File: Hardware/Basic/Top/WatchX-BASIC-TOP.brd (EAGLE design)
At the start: 0 parts

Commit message: followed along with Take 001
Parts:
- added C10, C11: 300p, LinnesLab-Passives:C0603
- added C12: 10u, LinnesLab-Passives:C0805
- added C13, C15, C17, C18, C19: 2.2uF, LinnesLab-Passives:C0402
- added C14: 100n, LinnesLab-Passives:C0603
- added C16: 10uF, LinnesLab-Passives:C0603
- added C2, C5, C6, C7: 1u, LinnesLab-Passives:C0603
- added C20, C21: 4.7u, LinnesLab-Passives:C0603
- added C8, C9: (no value), LinnesLab-Passives:C0603
- added CHRG2: MCP73831, LinnesLab-Power:SOT23-5
- added CORTEX1: CORTEX_DEBUG_PTH, LinnesLab-Connectors:2X5-PTH-1.27MM
- added D1, D4, D5: (no value), LinnesLab-DiscreteSemi:USC
- added J2: (no value), LinnesLab-Connectors:1X02
- added L2: 10u, LinnesLab-Passives:L0603
- added LDO2: MIC5504, LinnesLab-Power:SOT23-5
- added LED3: RED, LinnesLab-LED:LED-0603
- added LED4: BLUE, LinnesLab-LED:LED-0603
- added R11: (no value), LinnesLab-Passives:R0603
- added R12, R13, R14, R15: 100k, LinnesLab-Passives:R0603
- added R3, R4: 1k, LinnesLab-Passives:R0603
- added R5, R6, R8, R9: 10k, LinnesLab-Passives:R0603
- added R7: 390k, LinnesLab-Passives:R0603
- added SD2: (no value), LinnesLab-Connectors:MICROSD
- added SW1, SW2: SWITCH.MOM, LinnesLab-Switches:TACTILE_SWITCH_SMD_6.2MM_TALL
- added SW3, SW4: (no value), LinnesLab-Switches:BUTTON-GULLWING
- added U2: NRF52832_MODULE_MDBT42, LinnesLab-Microcontrollers:BLE_MODULE_RAYTAC_MDBT42
- added U3: (no value), LinnesLab-Displays:UG-2864HSWEG01_0.96IN_NO-WRAPAROUND
- added U4: PCF8523, LinnesLab-Clocks:SO8
- added USB2: USB.MICRO-BIGGERPADS, LinnesLab-Connectors:USB-MICRO-01.BIGGERPADS
- added XTAL2: 32.768kHz, LinnesLab-Clocks:2-SMD.NOLEAD.2.0MMTO1.2MM
- added XTAL3: 32.7680kHz, LinnesLab-Clocks:2-SMD.NOLEAD.2.0MMTO1.2MM
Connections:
- new net 3.3V: C12.2, C17.2, C19.2, C2.1, C6.1, CORTEX1.1, D1.-, LDO2.5, R15.2, R5.2, R8.2, R9.2, SD2.4, U2.11, U3.6, U3.9, U4.8
- new net BATT: R13.1, R14.2
- new net CD1: SD2.CD1
- new net CD2: SD2.CD2
- new net CHRG.STAT: CHRG2.1, R12.1
- new net CS.OLED: U3.13
- new net DC.OLED: U3.15
- new net DFU: SW3.3, U2.34
- new net DTR: C14.1
- new net FRST: U2.38
- new net GND: C10.2, C11.2, C12.1, C16.1, C17.1, C18.1, C19.1, C2.2, C20.2, C21.1, C5.1, C6.2, C7.2, C8.1, C9.2, CHRG2.2, CORTEX1.3, CORTEX1.5, CORTEX1.7, CORTEX1.9, J2.1, LDO2.2, LED3.C, LED4.C, R11.1, R14.1, R15.1, R6.1, R7.2, SD2.6, SD2.MT1, SD2.MT2, SW1.B1, SW1.B2, SW2.B1, SW2.B2, SW3.1, SW4.3, U2.1, U2.12, U2.24, U2.39, U3.1, U3.10, U3.12, U3.29, U3.30, U3.8, U4.4, USB2.5, USB2.S1, USB2.S2, USB2.S3, USB2.S4, USB2.S5, USB2.S6
- new net LED1: R3.2, U2.31
- new net LED2: R4.2, U2.33
- new net MISO: SD2.7, U2.28
- new net MOSI: SD2.3, U2.27, U3.19
- new net N$1: R6.2, U3.11
- new net N$10: LED4.A, R4.1
- new net N$11: L2.1, U2.10
- new net N$12: C7.1, L2.2, U2.9
- new net N$13: C16.2, U3.28
- new net N$14: CORTEX1.8
- new net N$15: C18.2, U3.27
- new net N$17: CHRG2.5, R11.2
- new net N$19: U4.2, XTAL3.P$1
- new net N$2: R7.1, U3.26
- new net N$20: U4.1, XTAL3.P$2
- new net N$3: C13.2, U3.2
- new net N$4: C8.2, U2.13, XTAL2.P$1
- new net N$5: C13.1, U3.3
- new net N$6: C9.1, U2.14, XTAL2.P$2
- new net N$7: C15.2, U3.4
- new net N$8: C15.1, U3.5
- new net N$9: LED3.A, R3.1
- new net P0.09/NFC1: C11.1, U2.22
- new net P0.10/NFC2: C10.1, U2.23
- new net RESET: C14.2, CORTEX1.10, D1.+, R5.1, SW4.1, U2.35
- new net RESET.OLED: U3.14
- new net RXD: U2.21
- new net SCK: SD2.5, U2.26, U3.18
- new net SCL: R8.1, U2.3, U4.6
- new net SD.CS: SD2.2
- new net SDA: R9.1, U2.2, U4.5
- new net SW1: SW1.A1, SW2.A1
- new net SWCLK: CORTEX1.4, U2.36
- new net SWDIO: CORTEX1.2, U2.37
- new net SWO: CORTEX1.6, U2.32
- new net TXD: U2.19
- new net USB+: USB2.3
- new net USB-: USB2.2
- new net VBATT: U4.3
- new net VIN: C21.2, C5.2, CHRG2.4, D4.-, D5.-, LDO2.1, LDO2.3, R12.2
- new net VLIPO: C20.1, CHRG2.3, D4.+, J2.2, R13.2
- new net V_USB: D5.+, USB2.1
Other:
- board outline added: 38 x 38 mm

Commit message: changes up to take 003
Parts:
- removed R8, R9: 10k, LinnesLab-Passives:R0603
- added C22: 100n, LinnesLab-Passives:C0603
- added C23, C24: 47p, LinnesLab-Passives:C0603
- added J3: (no value), LinnesLab-Connectors:1X07_1.27MM
- added JP2: (no value), LinnesLab-Switches:SMT-JUMPER_2_NO_SILK
- added LED5: RED, LinnesLab-LED:LED-0603
- added LED6: YELLOW, LinnesLab-LED:LED-0603
- added R1, R2: 10k, LinnesLab-Passives:R0603
- added R17, R18: 27, LinnesLab-Passives:R0603
- added R19, R20: 1k, LinnesLab-Passives:R0603
- added R21, R22: (no value), LinnesLab-Passives:R0603
- added U5: FT231XS, LinnesLab-DigitalIC:SSOP20_L
- moved R4 57.8 mm to (5.25, -19.0)
- moved R3 53.1 mm to (10.8, -19.5)
- moved SW4 37.3 mm to (73.4, 0.06)
- moved U4 37.3 mm to (27.1, -4.91)
- moved XTAL3 37.1 mm to (22.1, -3.55)
- moved LED3 35.2 mm to (74.1, 8.57)
- moved SW3 35.1 mm to (79.7, 14.7)
- moved LED4 34.8 mm to (73.8, 10.8)
- moved CORTEX1 34.1 mm to (71.2, 14.7)
- moved L2 33.3 mm to (51.0, 9.35)
- moved C2 31.5 mm to (9.35, -1.78)
- moved C8 29.3 mm to (54.3, 8.17)
- moved C7 29.1 mm to (50.7, 13.7)
- moved D5 27.1 mm to (24.7, -14.2)
- moved C9 26.6 mm to (54.8, 6.15)
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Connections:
- net CHRG.STAT renamed D27/CHRG.STAT
- removed net BATT: R13.1, R14.2
- removed net CD1: SD2.CD1
- removed net CS.OLED: U3.13
- removed net DC.OLED: U3.15
- removed net RESET.OLED: U3.14
- removed net SD.CS: SD2.2
- removed net SW1: SW1.A1, SW2.A1
- new net !CTS: JP2.2, U5.9
- new net !DTR: U5.1
- new net A4/BATT: R13.1, R14.2, U2.5
- new net A6/TIA: J3.6, U2.7
- new net A7/PPG: J3.7, U2.8
- new net D11/SW1: SW1.A1, U2.25
- new net D15/SW2: SW2.A1, U2.29
- new net D16/CS.OLED: U2.30, U3.13
- new net D27/CHRG.STATUS: U2.4
- new net D29/LED.CTRL: J3.5, U2.6
- new net D3/RESET.OLED: U2.17, U3.14
- new net D4/DC.OLED: U2.16, U3.15
- new net D5/CD1: SD2.CD1, U2.18
- new net D7/SD.CS: SD2.2, U2.20
- new net FT3V3: U5.13
- new net N$23: R17.2, U5.12
- new net N$24: R18.2, U5.11
- new net N$25: LED5.C, R19.2
- new net N$26: LED6.C, R20.2
- new net RXD.FT: R22.1
- new net RXD.NRF: R21.2, U2.21
- new net RXLED: R19.1, U5.17
- new net TXD.FT: R21.1
- new net TXD.NRF: R22.2, U2.19
- new net TXLED: R20.1, U5.10
- net 3.3V: now also C22.2, J3.4, LED5.A, LED6.A, R1.2, R2.2, U5.14, U5.3; no longer R8.2, R9.2
- net GND: now also C22.1, C23.2, C24.1, J3.3, JP2.1, U5.16, U5.6
- net RXD: now also U5.4; no longer U2.21
- net SCL: now also J3.2, R2.1; no longer R8.1
- net SDA: now also J3.1, R1.1; no longer R9.1
- net TXD: now also U5.20; no longer U2.19
- net USB+: now also C23.1, R18.1
- net USB-: now also C24.2, R17.1
- net V_USB: now also U5.15

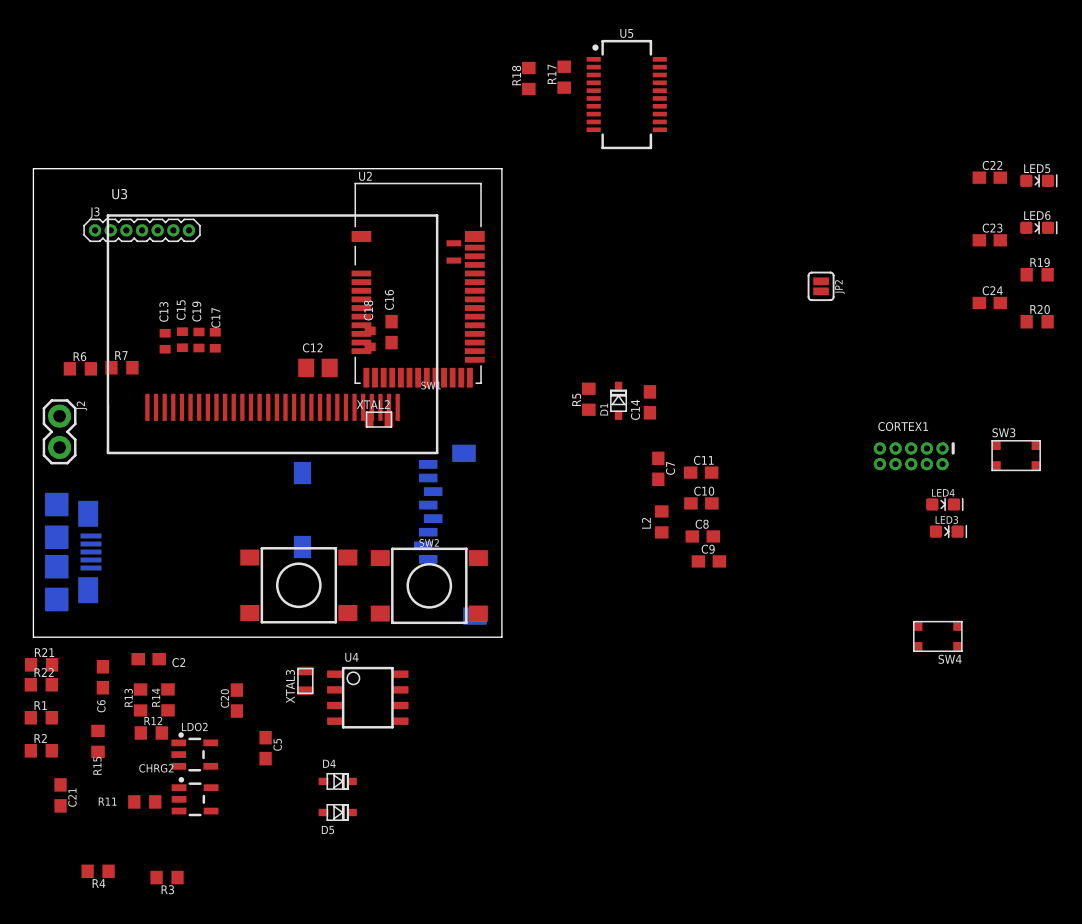
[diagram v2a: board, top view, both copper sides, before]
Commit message: edits through end of Take 008 video
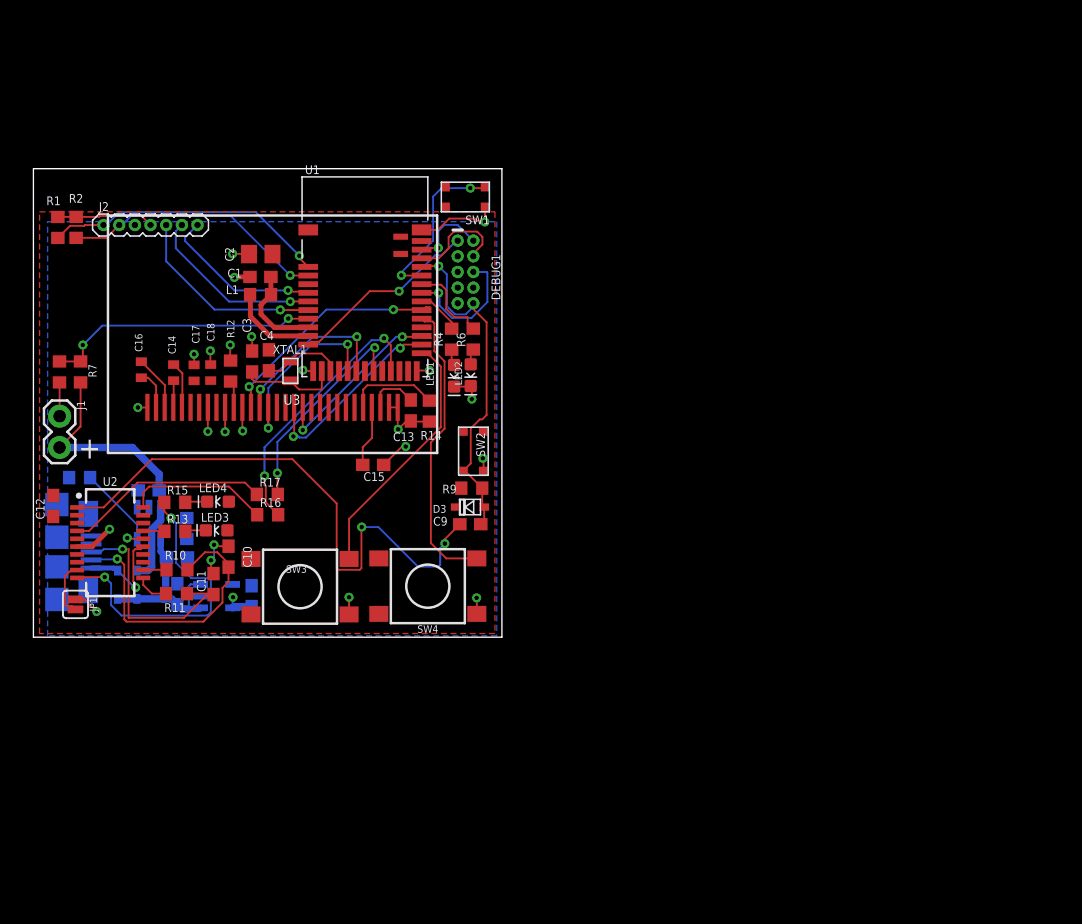
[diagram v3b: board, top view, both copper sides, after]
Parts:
- removed C19: 2.2uF, LinnesLab-Passives:C0402
- removed C20, C21: 4.7u, LinnesLab-Passives:C0603
- removed C22: 100n, LinnesLab-Passives:C0603
- removed C23, C24: 47p, LinnesLab-Passives:C0603
- removed CHRG2: MCP73831, LinnesLab-Power:SOT23-5
- removed CORTEX1: CORTEX_DEBUG_PTH, LinnesLab-Connectors:2X5-PTH-1.27MM
- removed D4, D5: (no value), LinnesLab-DiscreteSemi:USC
- removed J3: (no value), LinnesLab-Connectors:1X07_1.27MM
- removed JP2: (no value), LinnesLab-Switches:SMT-JUMPER_2_NO_SILK
- removed L2: 10u, LinnesLab-Passives:L0603
- removed LDO2: MIC5504, LinnesLab-Power:SOT23-5
- removed LED5: RED, LinnesLab-LED:LED-0603
- removed LED6: YELLOW, LinnesLab-LED:LED-0603
- removed R18: 27, LinnesLab-Passives:R0603
- removed R19, R20: 1k, LinnesLab-Passives:R0603
- removed R21, R22: (no value), LinnesLab-Passives:R0603
- removed SD2: (no value), LinnesLab-Connectors:MICROSD
- removed U4: PCF8523, LinnesLab-Clocks:SO8
- removed U5: FT231XS, LinnesLab-DigitalIC:SSOP20_L
- removed XTAL2: 32.768kHz, LinnesLab-Clocks:2-SMD.NOLEAD.2.0MMTO1.2MM
- removed XTAL3: 32.7680kHz, LinnesLab-Clocks:2-SMD.NOLEAD.2.0MMTO1.2MM
- added C1: 1u, LinnesLab-Passives:C0603
- added C3, C4: (no value), LinnesLab-Passives:C0603
- added CHRG1: MCP73831, LinnesLab-Power:SOT23-5
- added D2, D3: (no value), LinnesLab-DiscreteSemi:USC
- added DEBUG1: CORTEX_DEBUG_PTH, LinnesLab-Connectors:2X5-PTH-1.27MM
- added J1: (no value), LinnesLab-Connectors:1X02
- added JP1: (no value), LinnesLab-Switches:SMT-JUMPER_2_NO_SILK
- added L1: 10u, LinnesLab-Passives:L0603
- added LDO1: MIC5504, LinnesLab-Power:SOT23-5
- added LED1: RED, LinnesLab-LED:LED-0603
- added LED2: BLUE, LinnesLab-LED:LED-0603
- added R10: 27, LinnesLab-Passives:R0603
- added R16: (no value), LinnesLab-Passives:R0603
- added R8: 100k, LinnesLab-Passives:R0603
- added R9: 10k, LinnesLab-Passives:R0603
- added U1: NRF52832_MODULE_MDBT42, LinnesLab-Microcontrollers:BLE_MODULE_RAYTAC_MDBT42
- added XTAL1: 32.768kHz, LinnesLab-Clocks:2-SMD.NOLEAD.2.0MMTO1.2MM
- C10, C11: value 300p -> 47p
- C12: value 10u -> 100n; device LinnesLab-Passives:C0805 -> LinnesLab-Passives:C0603
- C13: value 2.2uF -> 10uF; device LinnesLab-Passives:C0402 -> LinnesLab-Passives:C0603
- C14: value 100n -> 2.2uF; device LinnesLab-Passives:C0603 -> LinnesLab-Passives:C0402
- C15: device LinnesLab-Passives:C0402 -> LinnesLab-Passives:C0603
- C16: value 10uF -> 2.2uF; device LinnesLab-Passives:C0603 -> LinnesLab-Passives:C0402
- C2: value 1u -> 10u; device LinnesLab-Passives:C0603 -> LinnesLab-Passives:C0805
- C5: value 1u -> 4.7u
- C8: value (none) -> 4.7u
- C9: value (none) -> 100n
- J2: device LinnesLab-Connectors:1X02 -> LinnesLab-Connectors:1X07_1.27MM
- LED4: value BLUE -> YELLOW
- R11: value (none) -> 27
- R12: value 100k -> 10k
- R13, R15: value 100k -> 1k
- R14: value 100k -> 390k
- R17: value 27 -> (none)
- R3: value 1k -> 100k
- R5: value 10k -> 5k
- R6: value 10k -> 1k
- R7: value 390k -> 100k
- SW1, SW2: value SWITCH.MOM -> (none); device LinnesLab-Switches:TACTILE_SWITCH_SMD_6.2MM_TALL -> LinnesLab-Switches:BUTTON-GULLWING
- SW3, SW4: value (none) -> SWITCH.MOM; device LinnesLab-Switches:BUTTON-GULLWING -> LinnesLab-Switches:TACTILE_SWITCH_SMD_6.2MM_TALL
- U2: value NRF52832_MODULE_MDBT42 -> FT231XS; device LinnesLab-Microcontrollers:BLE_MODULE_RAYTAC_MDBT42 -> LinnesLab-DigitalIC:SSOP20_L
- moved LED3 59.2 mm to (14.9, 8.67), turned to 180 degrees
- moved SW3 59.0 mm to (21.6, 4.10), turned to 180 degrees
- moved LED4 58.8 mm to (15.0, 11.0), turned to 180 degrees
- moved R4 51.8 mm to (33.9, 24.2), turned to 90 degrees
- moved C8 45.1 mm to (9.35, 11.9), flipped to the bottom
- moved R2 42.5 mm to (3.46, 33.2), turned to 90 degrees
- moved D1 41.8 mm to (8.40, 4.26), flipped to the bottom, turned to 270 degrees
- moved R5 41.8 mm to (3.74, 12.9), flipped to the bottom, turned to 180 degrees
- moved SW4 41.6 mm to (32.0, 4.14)
- moved R17 41.5 mm to (19.0, 11.6), turned to 0 degrees
- moved C11 40.6 mm to (14.6, 4.31), turned to 90 degrees
- moved R1 39.8 mm to (1.98, 33.2), turned to 90 degrees
- moved C14 38.7 mm to (11.4, 21.5)
- moved C10 38.6 mm to (15.8, 6.53), turned to 270 degrees
- moved C7 34.6 mm to (17.7, 3.33), flipped to the bottom, turned to 90 degrees
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- renumbered USB2 to USB1
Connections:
- removed net !DTR: U5.1
- removed net A4/BATT: R13.1, R14.2, U2.5
- removed net A6/TIA: J3.6, U2.7
- removed net A7/PPG: J3.7, U2.8
- removed net CD2: SD2.CD2
- removed net D29/LED.CTRL: J3.5, U2.6
- removed net N$19: U4.2, XTAL3.P$1
- removed net N$20: U4.1, XTAL3.P$2
- removed net RXD: U5.4
- removed net TXD: U5.20
- removed net VBATT: U4.3
- new net A4/PPG: J2.7, U1.5
- new net A5/TIA: J2.6, U1.6
- new net A7/BATT: R7.1, R8.2, U1.8
- new net D30/LED.CTRL: J2.5, U1.7
- net !CTS: now also JP1.2, U2.9; no longer JP2.2, U5.9
- net 3.3V: now also C18.2, C2.2, C7.1, D3.-, DEBUG1.1, J2.4, LDO1.5, LED3.A, LED4.A, R9.2, U1.11, U2.14, U2.3; no longer C19.2, C2.1, C22.2, C6.1, CORTEX1.1, D1.-, J3.4, LDO2.5, LED5.A, LED6.A, R15.2, R5.2, SD2.4, U2.11, U4.8, U5.14, U5.3
- net D11/SW1: now also SW3.A1, U1.25; no longer SW1.A1, U2.25
- net D15/SW2: now also SW4.A1, U1.29; no longer SW2.A1, U2.29
- net D16/CS.OLED: now also U1.30; no longer U2.30
- net D27/CHRG.STAT: now also CHRG1.1, R3.1; no longer CHRG2.1, R12.1
- net D27/CHRG.STATUS: now also U1.4; no longer U2.4
- net D3/RESET.OLED: now also U1.17; no longer U2.17
- net D4/DC.OLED: now also U1.16; no longer U2.16
- net D5/CD1: now also U1.18; no longer SD2.CD1, U2.18
- net D7/SD.CS: now also U1.20; no longer SD2.2, U2.20
- net DFU: now also SW1.3, U1.34; no longer SW3.3, U2.34
- net DTR: now also C9.1, U2.1; no longer C14.1
- net FRST: now also U1.38; no longer U2.38
- net FT3V3: now also U2.13; no longer U5.13
- net GND: now also C1.2, C10.1, C13.1, C15.1, C2.1, C3.1, C4.2, C6.1, C8.2, CHRG1.2, DEBUG1.3, DEBUG1.5, DEBUG1.7, DEBUG1.9, J1.1, J2.3, JP1.1, LDO1.2, LED1.C, LED2.C, R12.1, R14.2, R5.1, R8.1, SW1.1, SW2.3, SW3.B1, SW3.B2, SW4.B1, SW4.B2, U1.1, U1.12, U1.24, U1.39, U2.16, U2.6; no longer C10.2, C16.1, C19.1, C2.2, C20.2, C21.1, C22.1, C23.2, C24.1, C6.2, C8.1, C9.2, CHRG2.2, CORTEX1.3, CORTEX1.5, CORTEX1.7, CORTEX1.9, J2.1, J3.3, JP2.1, LDO2.2, LED3.C, LED4.C, R11.1, R14.1, R15.1, R6.1, R7.2, SD2.6, SD2.MT1, SD2.MT2, SW1.B1, SW1.B2, SW2.B1, SW2.B2, SW3.1, SW4.3, U2.1, U2.12, U2.24, U2.39, U4.4, U5.16, U5.6
- net LED1: now also R4.2, U1.31; no longer R3.2, U2.31
- net LED2: now also R6.2, U1.33; no longer R4.2, U2.33
- net MISO: now also U1.28; no longer SD2.7, U2.28
- net MOSI: now also U1.27; no longer SD2.3, U2.27
- net N$1: now also R12.2; no longer R6.2
- net N$10: now also LED2.A, R6.1; no longer LED4.A, R4.1
- net N$11: now also L1.1, U1.10; no longer L2.1, U2.10
- net N$12: now also C1.1, L1.2, U1.9; no longer C7.1, L2.2, U2.9
- net N$13: now also C13.2; no longer C16.2
- net N$14: now also DEBUG1.8; no longer CORTEX1.8
- net N$15: now also C15.2; no longer C18.2
- net N$17: now also CHRG1.5, R5.2; no longer CHRG2.5, R11.2
- net N$2: now also R14.1; no longer R7.1
- net N$23: now also R10.2, U2.12; no longer R17.2, U5.12
- net N$24: now also R11.2, U2.11; no longer R18.2, U5.11
- net N$25: now also LED3.C, R13.2; no longer LED5.C, R19.2
- net N$26: now also LED4.C, R15.2; no longer LED6.C, R20.2
- net N$3: now also C16.2; no longer C13.2
- net N$4: now also C3.2, U1.13, XTAL1.P$1; no longer C8.2, U2.13, XTAL2.P$1
- net N$5: now also C16.1; no longer C13.1
- net N$6: now also C4.1, U1.14, XTAL1.P$2; no longer C9.1, U2.14, XTAL2.P$2
- net N$7: now also C14.2; no longer C15.2
- net N$8: now also C14.1; no longer C15.1
- net N$9: now also LED1.A, R4.1; no longer LED3.A, R3.1
- net P0.09/NFC1: now also U1.22; no longer C11.1, U2.22
- net P0.10/NFC2: now also U1.23; no longer C10.1, U2.23
- net RESET: now also C9.2, D3.+, DEBUG1.10, R9.1, SW2.1, U1.35; no longer C14.2, CORTEX1.10, D1.+, R5.1, SW4.1, U2.35
- net RXD.FT: now also R17.1, U2.4; no longer R22.1
- net RXD.NRF: now also R16.2, U1.21; no longer R21.2, U2.21
- net RXLED: now also R13.1, U2.17; no longer R19.1, U5.17
- net SCK: now also U1.26; no longer SD2.5, U2.26
- net SCL: now also J2.2, U1.3; no longer J3.2, U2.3, U4.6
- net SDA: now also J2.1, U1.2; no longer J3.1, U2.2, U4.5
- net SWCLK: now also DEBUG1.4, U1.36; no longer CORTEX1.4, U2.36
- net SWDIO: now also DEBUG1.2, U1.37; no longer CORTEX1.2, U2.37
- net SWO: now also DEBUG1.6, U1.32; no longer CORTEX1.6, U2.32
- net TXD.FT: now also R16.1, U2.20; no longer R21.1
- net TXD.NRF: now also R17.2, U1.19; no longer R22.2, U2.19
- net TXLED: now also R15.1, U2.10; no longer R20.1, U5.10
- net USB+: now also C11.1, R11.1; no longer C23.1, R18.1
- net USB-: now also C10.2, R10.1; no longer C24.2, R17.1
- net VIN: now also C6.2, CHRG1.4, D1.-, D2.-, LDO1.1, LDO1.3, R3.2; no longer C21.2, CHRG2.4, D4.-, D5.-, LDO2.1, LDO2.3, R12.2
- net VLIPO: now also C8.1, CHRG1.3, D1.+, J1.2, R7.2; no longer C20.1, CHRG2.3, D4.+, J2.2, R13.2
- net V_USB: now also D2.+, U2.15; no longer D5.+, U5.15
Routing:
- net GND: track 0.00 -> 50.0 mm, vias 0 -> 24
- net DTR: track 0.00 -> 46.6 mm, vias 0 -> 2
- net RESET: track 0.00 -> 28.5 mm, vias 0 -> 1
- net 3.3V: track 0.00 -> 26.5 mm, vias 0 -> 2
- net TXLED: track 0.00 -> 24.6 mm, vias 0 -> 2
- net D15/SW2: track 0.00 -> 24.1 mm
- net USB-: track 0.00 -> 23.7 mm, vias 0 -> 1
- net SDA: track 0.00 -> 23.1 mm, vias 0 -> 1
- net VLIPO: track 0.00 -> 22.7 mm
- net A7/BATT: track 0.00 -> 22.3 mm, vias 0 -> 2
- net RXD.NRF: track 0.00 -> 22.2 mm, vias 0 -> 2
- net SCL: track 0.00 -> 21.6 mm, vias 0 -> 1
- net D11/SW1: track 0.00 -> 20.9 mm
- net D16/CS.OLED: track 0.00 -> 19.8 mm, vias 0 -> 2
- net USB+: track 0.00 -> 18.2 mm, vias 0 -> 1
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- added copper zone on layer 1, net 3.3V
- added copper zone on layer 16, net GND
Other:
- board text added: "+"
